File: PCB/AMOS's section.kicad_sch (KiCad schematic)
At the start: 15 parts, among them J1 USB_C_Receptacle_PowerOnly_6P, J2 Conn_02x16_Odd_Even, U6 TP4056-42-ESOP8, U7 CH224K, U8 TS5A3159ADBVR

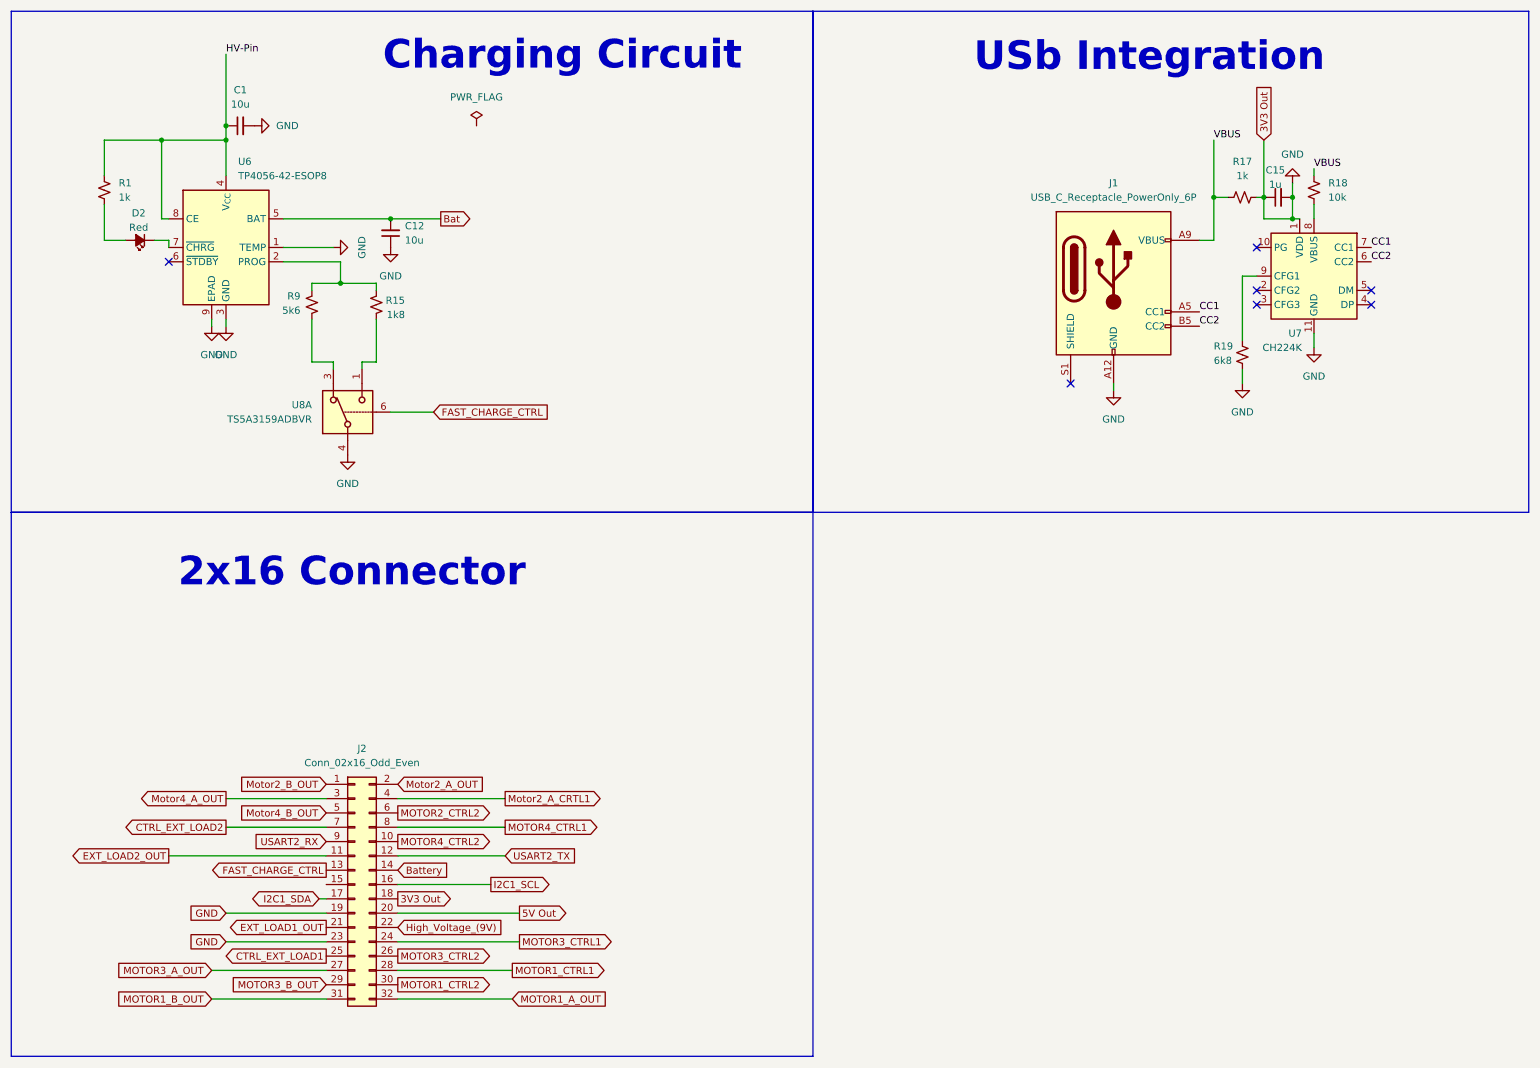
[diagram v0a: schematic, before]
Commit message: Fix passive components footprints
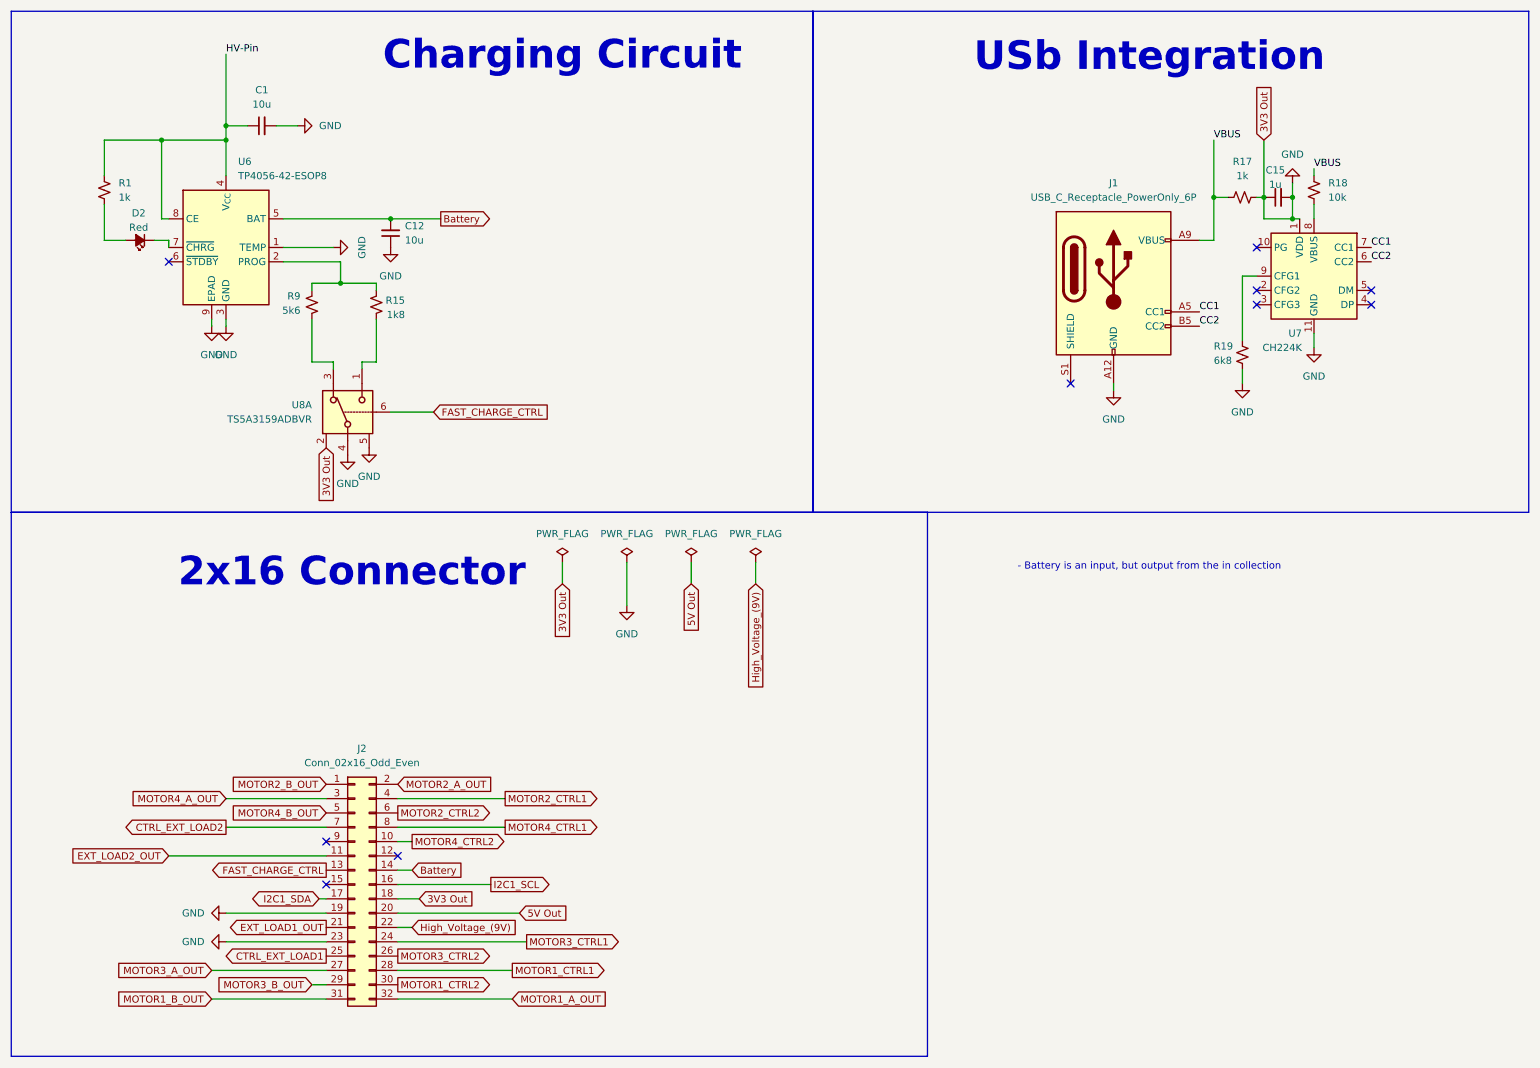
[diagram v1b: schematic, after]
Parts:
- C1, C12, C15: footprint Nhlamolo.:C1206 -> Capacitor_SMD:C_1206_3216Metric_Pad1.33x1.80mm_HandSolder
- D2: footprint Nhlamolo.:LED0603-RD -> LED_SMD:LED_0603_1608Metric_Pad1.05x0.95mm_HandSolder
- R1, R17: footprint Nhlamolo.:R0402 -> Resistor_SMD:R_0402_1005Metric_Pad0.72x0.64mm_HandSolder
- R15: footprint Nhlamolo.:R0603 -> Resistor_SMD:R_0603_1608Metric_Pad0.98x0.95mm_HandSolder
- R18, R19, R9: footprint Nhlamolo.:R0805 -> Resistor_SMD:R_0805_2012Metric_Pad1.20x1.40mm_HandSolder
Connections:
- net Bat is gone; now on net Battery: C12.2, U6.5 (BAT)
- net GND: now also U8.2, U8.5
- net Motor2_A_CRTL1 renamed MOTOR2_CTRL1
- net Motor2_A_OUT renamed MOTOR2_A_OUT
- net Motor2_B_OUT renamed MOTOR2_B_OUT
- net Motor4_A_OUT renamed MOTOR4_A_OUT
- net Motor4_B_OUT renamed MOTOR4_B_OUT
- net USART2_RX: no longer names the net of J2.9 (Pin_9)
- net USART2_TX: no longer names the net of J2.12 (Pin_12)
- no-connect marks 7 -> 10
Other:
- note added: "- Battery is an input, but output from the in collection"
- moved on the sheet: C1

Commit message: Error Resolutions
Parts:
- removed C1, C12: 10u, Capacitor_SMD:C_1206_3216Metric_Pad1.33x1.80mm_HandSolder, symbol Device:C_Small
- removed C15: 1u, Capacitor_SMD:C_1206_3216Metric_Pad1.33x1.80mm_HandSolder, symbol Device:C_Small
- removed D2: Red, LED_SMD:LED_0603_1608Metric_Pad1.05x0.95mm_HandSolder, symbol Device:LED_Small_Filled
- removed J1: USB_C_Receptacle_PowerOnly_6P, Nhlamolo.:USB-C-SMD_TYPE-602-T3, symbol Connector:USB_C_Receptacle_PowerOnly_6P
- removed J2: Conn_02x16_Odd_Even, symbol Connector_Generic:Conn_02x16_Odd_Even
- removed R1, R17: 1k, Resistor_SMD:R_0402_1005Metric_Pad0.72x0.64mm_HandSolder, symbol Device:R_Small_US
- removed R15: 1k8, Resistor_SMD:R_0603_1608Metric_Pad0.98x0.95mm_HandSolder, symbol Device:R_Small_US
- removed R18: 10k, Resistor_SMD:R_0805_2012Metric_Pad1.20x1.40mm_HandSolder, symbol Device:R_Small_US
- removed R19: 6k8, Resistor_SMD:R_0805_2012Metric_Pad1.20x1.40mm_HandSolder, symbol Device:R_Small_US
- removed R9: 5k6, Resistor_SMD:R_0805_2012Metric_Pad1.20x1.40mm_HandSolder, symbol Device:R_Small_US
- removed U6: TP4056-42-ESOP8, Nhlamolo.:ESOP-8_L4.9-W3.9-P1.27-LS6.0-BL-EP-1, symbol Battery_Management:TP4056-42-ESOP8
- removed U7: CH224K, Nhlamolo.:ESSOP-10_L4.9-W3.9-P1.0-LS6.0-TL-EP, symbol Interface_USB:CH224K
- removed U8: TS5A3159ADBVR, Nhlamolo.:SOT-23-6_L2.9-W1.6-P0.95-LS2.8-BR, symbol Analog_Switch:TS5A3159ADBVR
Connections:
- no-connect marks 10 -> 0
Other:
- note removed: "- Battery is an input, but output from the in collection"
- note removed: "2x16 Connector"
- note removed: "Charging Circuit"
- note removed: "USb Integration"

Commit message: Final Schematic edits
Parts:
- added C21, C30: 10u, Capacitor_SMD:C_0603_1608Metric_Pad1.08x0.95mm_HandSolder, symbol Device:C_Small
- added C23: 1u, Capacitor_SMD:C_0603_1608Metric_Pad1.08x0.95mm_HandSolder, symbol Device:C_Small
- added D7: Red, LED_SMD:LED_0603_1608Metric_Pad1.05x0.95mm_HandSolder, symbol Device:LED_Small_Filled
- added J3: Conn_01x02_Pin, Connector_JST:JST_PH_S2B-PH-K_1x02_P2.00mm_Horizontal, symbol Connector:Conn_01x02_Pin
- added J6: USB_C_Receptacle_PowerOnly_6P, Mix:USB-C-SMD_TYPE-602-T3, symbol Connector:USB_C_Receptacle_PowerOnly_6P
- added JP17, JP30, JP31, JP32: Jumper_2_Small_Open, Jumper:SolderJumper-2_P1.3mm_Open_Pad1.0x1.5mm, symbol Jumper:Jumper_2_Small_Open
- added R16, R38: 1k, Resistor_SMD:R_0603_1608Metric_Pad0.98x0.95mm_HandSolder, symbol Device:R_Small_US
- added R19, R40: 10k, Resistor_SMD:R_0805_2012Metric_Pad1.20x1.40mm_HandSolder, symbol Device:R_Small_US
- added R20: 8.2k, Resistor_SMD:R_0805_2012Metric_Pad1.20x1.40mm_HandSolder, symbol Device:R_Small_US
- added R22: 5k6, Resistor_SMD:R_0805_2012Metric_Pad1.20x1.40mm_HandSolder, symbol Device:R_Small_US
- added R27: 1k8, Resistor_SMD:R_0603_1608Metric_Pad0.98x0.95mm_HandSolder, symbol Device:R_Small_US
- added R39: 6k8, Resistor_SMD:R_0805_2012Metric_Pad1.20x1.40mm_HandSolder, symbol Device:R_Small_US
- added SW3: SW_Nidec_CAS-120A1, Mix:SW-TH_1MS1T1B1M1QES-5, symbol Switch:SW_Nidec_CAS-120A1
- added TP10, TP26, TP42, TP8, TP9: TestPoint, TestPoint:TestPoint_Pad_D1.0mm, symbol Connector:TestPoint
- added U13: TP4056-42-ESOP8, Mix:ESOP-8_L4.9-W3.9-P1.27-LS6.0-BL-EP, symbol Battery_Management:TP4056-42-ESOP8
- added U15: CH224K, Mix:ESSOP-10_L4.9-W3.9-P1.0-LS6.0-TL-EP, symbol Interface_USB:CH224K
- added U8: TS5A3159ADBVR, Mix:SOT-23-6_L2.9-W1.6-P0.95-LS2.8-BR, symbol Symbols:TS5A3159ADBVR
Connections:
- new net: C30.2, JP31.2 (B), TP8.1, U13.5 (BAT)
- new net: C21.1, JP17.1 (A), R16.1, U13.4 (V_{CC}), U13.8 (CE)
- new net: D7.2 (A), R16.2
- new net: R27.2, U8.1 (NO)
- new net: R22.2, U8.3 (NC)
- new net: U13.2 (PROG), U8.4 (COM)
- new net: JP30.2 (B), U8.5 (V+)
- new net: D7.1 (K), U13.7 (~{CHRG})
- new net: C23.1, JP32.1 (A), R38.2, U15.1 (VDD)
- new net: J3.1 (Pin_1), SW3.2 (B)
- new net: R40.1, U15.8 (VBUS)
- new net: R39.2, U15.9 (CFG1)
- new net: JP17.2 (B), R19.2, R20.1, TP42.1
- new net 3V3 Out: JP30.1 (A)
- new net 3V3_Out: JP32.2 (B), TP26.1
- new net Battery: SW3.1 (C)
- new net CC1: J6.A5 (CC1), U15.7 (CC1)
- new net CC2: J6.B5 (CC2), U15.6 (CC2)
- new net Charger: JP31.1 (A), SW3.3 (A)
- new net FAST_CHARGE_CTRL: U8.6 (IN)
- new net GND: C21.2, C23.2, C30.1, J3.2 (Pin_2), J6.A12 (GND), J6.B12 (GND), R20.2, R22.1, R27.1, R39.1, U13.1 (TEMP), U13.3 (GND), U13.9 (EPAD), U15.11 (GND), U8.2 (GND)
- new net High_Voltage_(9V): J6.A9 (VBUS), J6.B9 (VBUS), R19.1, R38.1, R40.2, TP10.1, TP9.1
- no-connect marks 0 -> 7
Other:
- note added: "Charging Circuit"
- note added: "USb Integration"
